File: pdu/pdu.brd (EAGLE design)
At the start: 17.5 x 90 mm, 14 parts, among them IC1 FDN359BN, IC2 FDN359BN, IC3 FDN359BN

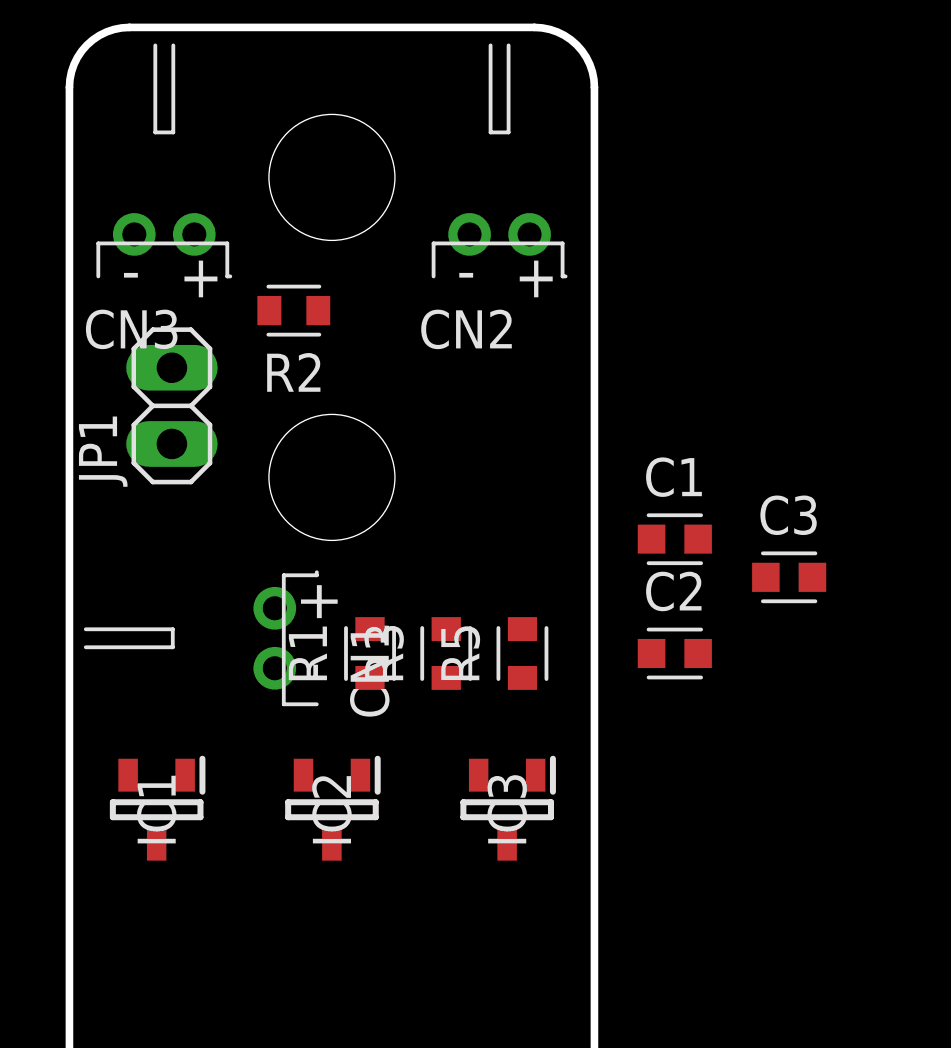
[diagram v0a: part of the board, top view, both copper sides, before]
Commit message: fix hole position
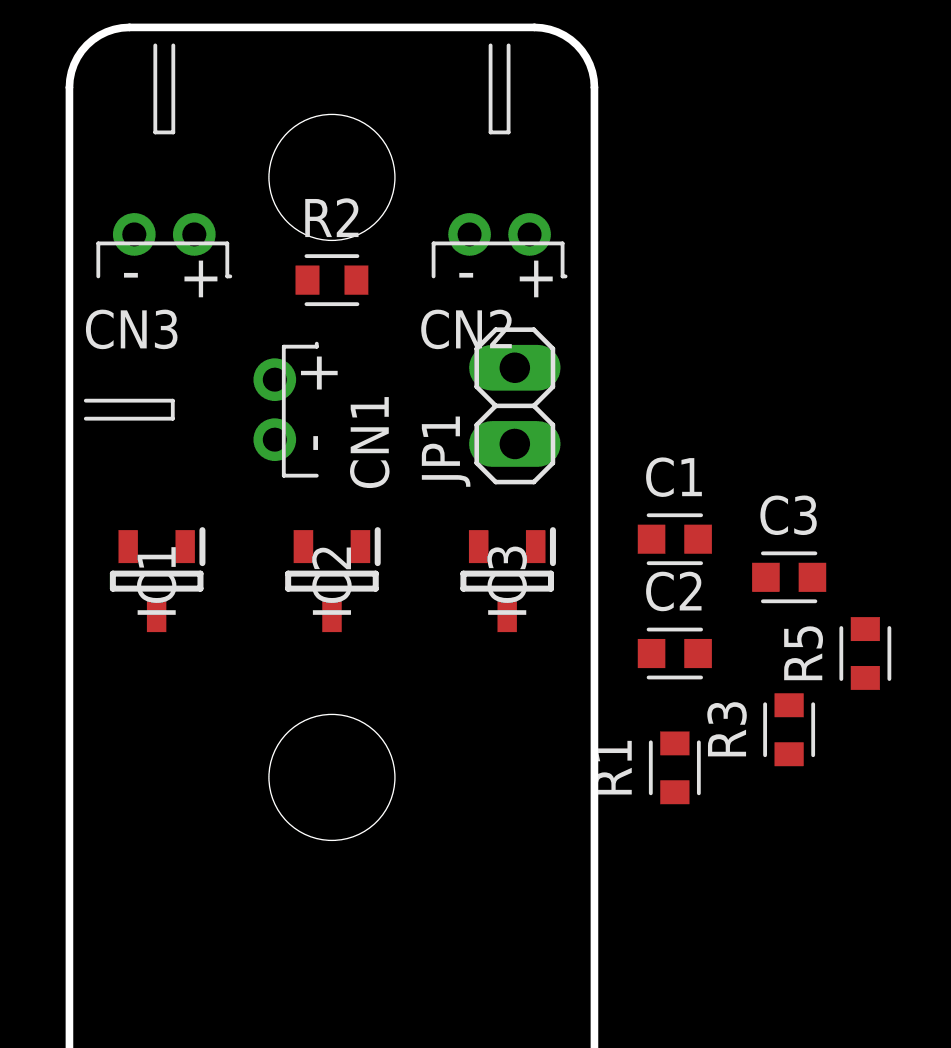
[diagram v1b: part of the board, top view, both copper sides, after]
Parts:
- moved R3 11.7 mm to (15.2, 21.6)
- moved R5 11.4 mm to (17.8, 24.1)
- moved JP1 11.4 mm to (6.10, 32.4)
- moved R1 10.9 mm to (11.4, 20.3)
- moved CN1 7.62 mm to (-1.91, 32.3)
- moved IC1 7.62 mm to (-5.84, 26.5)
- moved IC2 7.62 mm to (0.00, 26.5)
- moved IC3 7.62 mm to (5.84, 26.5)
- moved R2 1.63 mm to (0.00, 36.6), turned to 0 degrees

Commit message: add usb c (optional)
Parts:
- added C14: 100n, Capacitor:CAPC1608X85
- added C15: 1u, Capacitor:CAPC1608X85
- added D2: USBDiode, adafruit:SOD-123FL
- added J6: USB4105-GF-A, USB4105-GF-A:GCT_USB4105-GF-A
- added R12, R14: 5k1, Resistor:RESC1608X60
- added R13: 1M, Resistor:RESC1608X60
- moved C1 17.3 mm to (-5.84, 27.9)
- moved R5 16.0 mm to (2.92, 30.0)
- moved R1 15.7 mm to (-2.92, 26.7)
- moved R3 13.3 mm to (2.92, 26.7)
- moved C2 12.0 mm to (0.00, 27.9)
- moved C3 9.47 mm to (5.84, 27.8)
- moved IC3 1.78 mm to (5.84, 24.8)
- moved IC1 1.65 mm to (-5.84, 24.9)
- moved IC2 1.65 mm to (0.00, 24.9)
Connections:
- net N$4 renamed RET
- new net CC1: J6.A5, R14.1
- new net CC2: J6.B5, R12.1
- new net SHLD: J6.SH1, J6.SH2, J6.SH3, J6.SH4, R13.1
- new net VBUS: C14.2, C15.2, D2.A, J6.A4_B9, J6.B4_A9
- net GND: now also C14.1, C15.1, J6.A1_B12, J6.B1_A12, R12.2, R13.2, R14.2
- net VBAT: now also D2.C

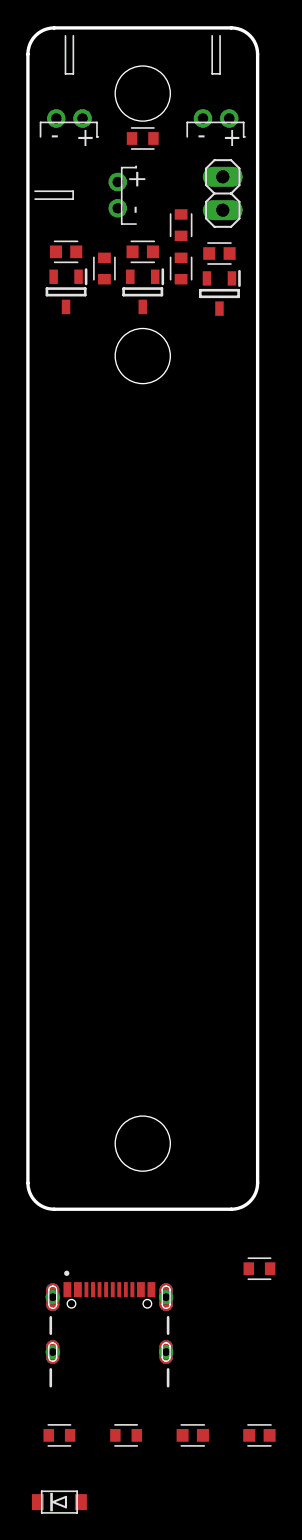
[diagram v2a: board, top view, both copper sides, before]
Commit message: add output with decoupling cap
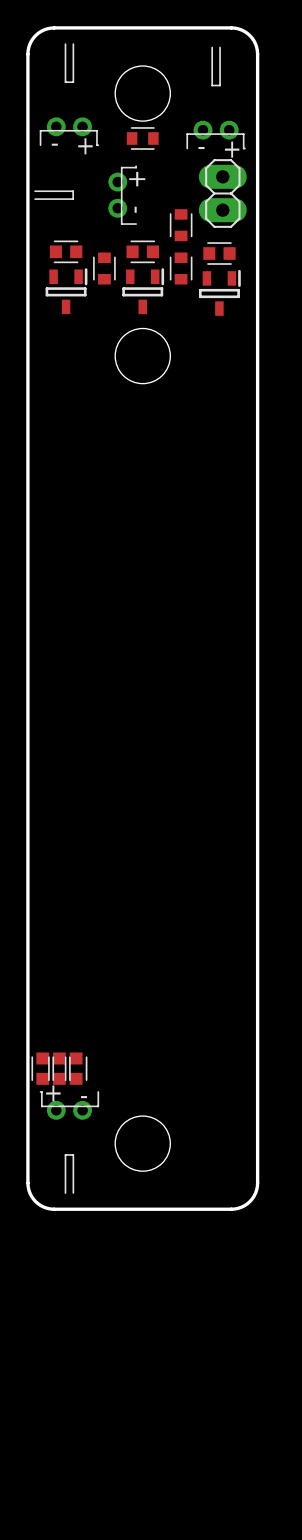
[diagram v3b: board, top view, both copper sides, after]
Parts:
- removed C14: 100n, Capacitor:CAPC1608X85
- removed C15: 1u, Capacitor:CAPC1608X85
- removed D2: USBDiode, adafruit:SOD-123FL
- removed J6: USB4105-GF-A, USB4105-GF-A:GCT_USB4105-GF-A
- removed R12, R14: 5k1, Resistor:RESC1608X60
- removed R13: 1M, Resistor:RESC1608X60
- added C4: 100n, Capacitor:CAPC1608X85
- added C5: 1u, Capacitor:CAPC1608X85
- added C6: 22u, Capacitor:CAPC1608X85
- added CN4: (no value), adafruit:JST-PH-2-THM-RA
- moved CN2 0.89 mm to (5.59, 37.2)
- moved CN3 0.63 mm to (-5.59, 37.5)
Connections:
- removed net CC1: J6.A5, R14.1
- removed net CC2: J6.B5, R12.1
- removed net SHLD: J6.SH1, J6.SH2, J6.SH3, J6.SH4, R13.1
- removed net VBUS: C14.2, C15.2, D2.A, J6.A4_B9, J6.B4_A9
- net GND: no longer C14.1, C15.1, J6.A1_B12, J6.B1_A12, R12.2, R13.2, R14.2
- net RET: now also C4.1, C5.1, C6.1, CN4.1
- net VBAT: now also C4.2, C5.2, C6.2, CN4.2; no longer D2.C

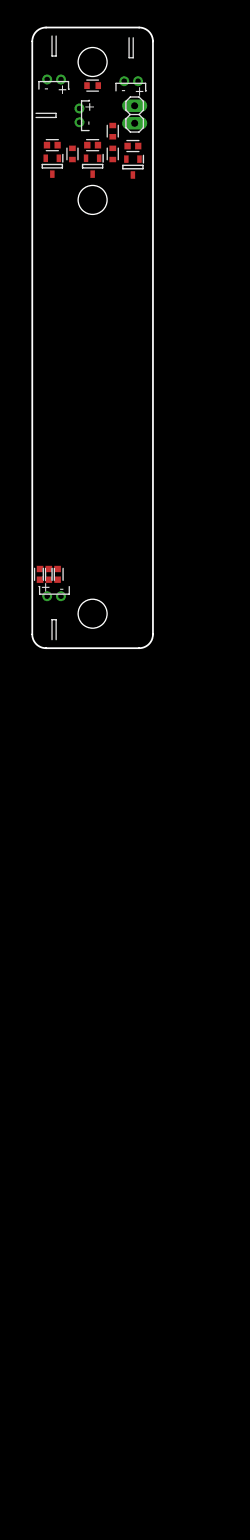
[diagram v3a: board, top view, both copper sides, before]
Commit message: fill length with conns
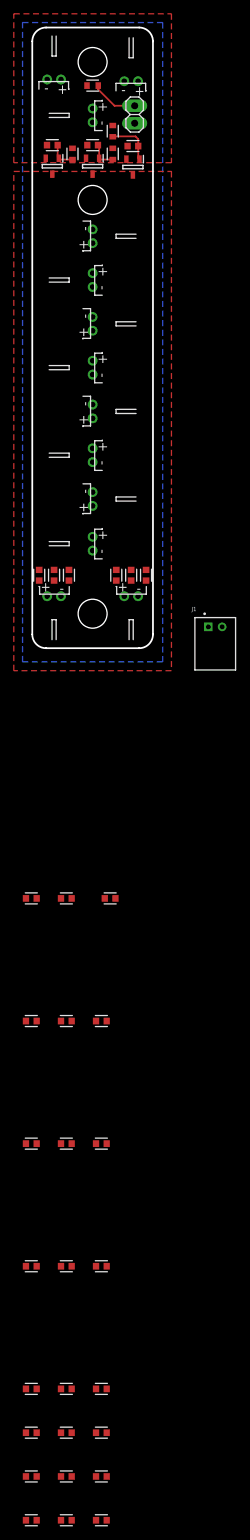
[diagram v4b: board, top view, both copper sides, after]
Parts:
- added C10, C13, C16, C19, C22, C25, C28, C31, C7: 100n, Capacitor:CAPC1608X85
- added C11, C14, C17, C20, C23, C26, C29, C32, C8: 1u, Capacitor:CAPC1608X85
- added C12, C15, C18, C21, C24, C27, C30, C33, C9: 22u, Capacitor:CAPC1608X85
- added CN10, CN11, CN12, CN13, CN5, CN6, CN7, CN8, CN9: (no value), adafruit:JST-PH-2-THM-RA
- added J1: S2B-PH-K-S(LF)(SN), Connectors:S2B-PH-K-S(LF)(SN)
- moved CN1 1.91 mm to (0.00, 32.3)
- moved C6 1.66 mm to (-3.43, -34.4)
- moved C5 0.77 mm to (-5.59, -34.4)
- moved C4 0.18 mm to (-7.75, -34.4)
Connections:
- net RET: now also C10.1, C11.1, C12.1, C13.1, C14.1, C15.1, C16.1, C17.1, C18.1, C19.1, C20.1, C21.1, C22.1, C23.1, C24.1, C25.1, C26.1, C27.1, C28.1, C29.1, C30.1, C31.1, C32.1, C33.1, C7.1, C8.1, C9.1, CN10.1, CN11.1, CN12.1, CN13.1, CN5.1, CN6.1, CN7.1, CN8.1, CN9.1
- net VBAT: now also C10.2, C11.2, C12.2, C13.2, C14.2, C15.2, C16.2, C17.2, C18.2, C19.2, C20.2, C21.2, C22.2, C23.2, C24.2, C25.2, C26.2, C27.2, C28.2, C29.2, C30.2, C31.2, C32.2, C33.2, C7.2, C8.2, C9.2, CN10.2, CN11.2, CN12.2, CN13.2, CN5.2, CN6.2, CN7.2, CN8.2, CN9.2
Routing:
- net EN: track 0.00 -> 7.17 mm
- net N$3: track 0.00 -> 6.85 mm
- net N$2: track 0.00 -> 4.02 mm
- net N$1: track 0.00 -> 4.02 mm
- added copper zone on layer 1, net GND
- added copper zone on layer 1, net RET
- added copper zone on layer 16, net VBAT

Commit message: swap connector
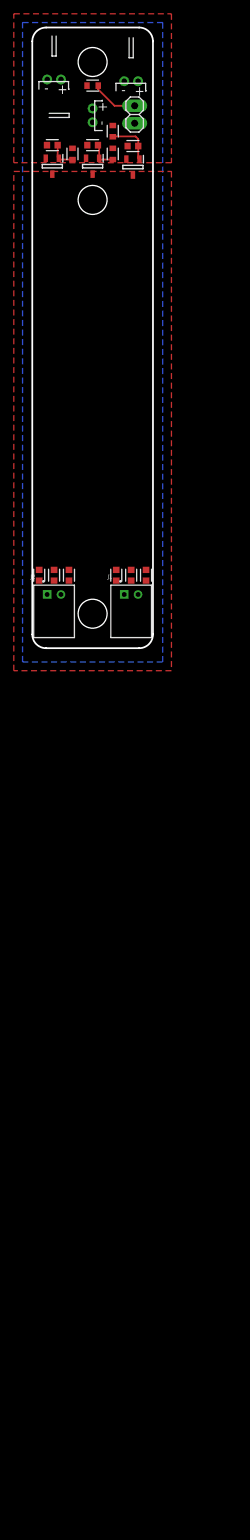
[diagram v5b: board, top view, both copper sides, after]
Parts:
- removed C10, C13, C16, C19, C22, C25, C28, C31: 100n, Capacitor:CAPC1608X85
- removed C11, C14, C17, C20, C23, C26, C29, C32: 1u, Capacitor:CAPC1608X85
- removed C12, C15, C18, C21, C24, C27, C30, C33: 22u, Capacitor:CAPC1608X85
- removed CN10, CN11, CN12, CN13, CN4, CN5, CN6, CN7, CN8, CN9: (no value), adafruit:JST-PH-2-THM-RA
- added J2: S2B-PH-K-S(LF)(SN), Connectors:S2B-PH-K-S(LF)(SN)
- moved J1 13.1 mm to (5.59, -37.2)
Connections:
- net RET: now also J1.1, J2.1; no longer C10.1, C11.1, C12.1, C13.1, C14.1, C15.1, C16.1, C17.1, C18.1, C19.1, C20.1, C21.1, C22.1, C23.1, C24.1, C25.1, C26.1, C27.1, C28.1, C29.1, C30.1, C31.1, C32.1, C33.1, CN10.1, CN11.1, CN12.1, CN13.1, CN4.1, CN5.1, CN6.1, CN7.1, CN8.1, CN9.1
- net VBAT: now also J1.2, J2.2; no longer C10.2, C11.2, C12.2, C13.2, C14.2, C15.2, C16.2, C17.2, C18.2, C19.2, C20.2, C21.2, C22.2, C23.2, C24.2, C25.2, C26.2, C27.2, C28.2, C29.2, C30.2, C31.2, C32.2, C33.2, CN10.2, CN11.2, CN12.2, CN13.2, CN4.2, CN5.2, CN6.2, CN7.2, CN8.2, CN9.2

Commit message: fully populate board
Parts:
- added C10, C13, C16, C19, C22, C25, C28, C31: 100n, Capacitor:CAPC1608X85
- added C11, C14, C17, C20, C23, C26, C29, C32: 1u, Capacitor:CAPC1608X85
- added C12, C15, C18, C21, C24, C27, C30, C33: 22u, Capacitor:CAPC1608X85
- added J10, J3, J4, J5, J6, J7, J8, J9: S2B-PH-K-S(LF)(SN), Connectors:S2B-PH-K-S(LF)(SN)
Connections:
- net RET: now also C10.1, C11.1, C12.1, C13.1, C14.1, C15.1, C16.1, C17.1, C18.1, C19.1, C20.1, C21.1, C22.1, C23.1, C24.1, C25.1, C26.1, C27.1, C28.1, C29.1, C30.1, C31.1, C32.1, C33.1, J10.1, J3.1, J4.1, J5.1, J6.1, J7.1, J8.1, J9.1
- net VBAT: now also C10.2, C11.2, C12.2, C13.2, C14.2, C15.2, C16.2, C17.2, C18.2, C19.2, C20.2, C21.2, C22.2, C23.2, C24.2, C25.2, C26.2, C27.2, C28.2, C29.2, C30.2, C31.2, C32.2, C33.2, J10.2, J3.2, J4.2, J5.2, J6.2, J7.2, J8.2, J9.2

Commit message: optimise layout
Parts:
- turned C10 to 180 degrees
- turned C11 to 180 degrees
- turned C12 to 180 degrees
- turned C13 to 180 degrees
- turned C14 to 180 degrees
- turned C15 to 180 degrees
- turned C16 to 180 degrees
- turned C17 to 180 degrees
- turned C18 to 180 degrees
- turned C19 to 180 degrees
- turned C20 to 180 degrees
- turned C21 to 180 degrees
